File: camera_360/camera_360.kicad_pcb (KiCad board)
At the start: 2 copper layers, 58 x 46 mm, 20 parts, among them J1 usb_cam3, J2 usb_cam2, J3 usb_cam1, J5 usb_in, U1 CH334R, Y1 12Mhz

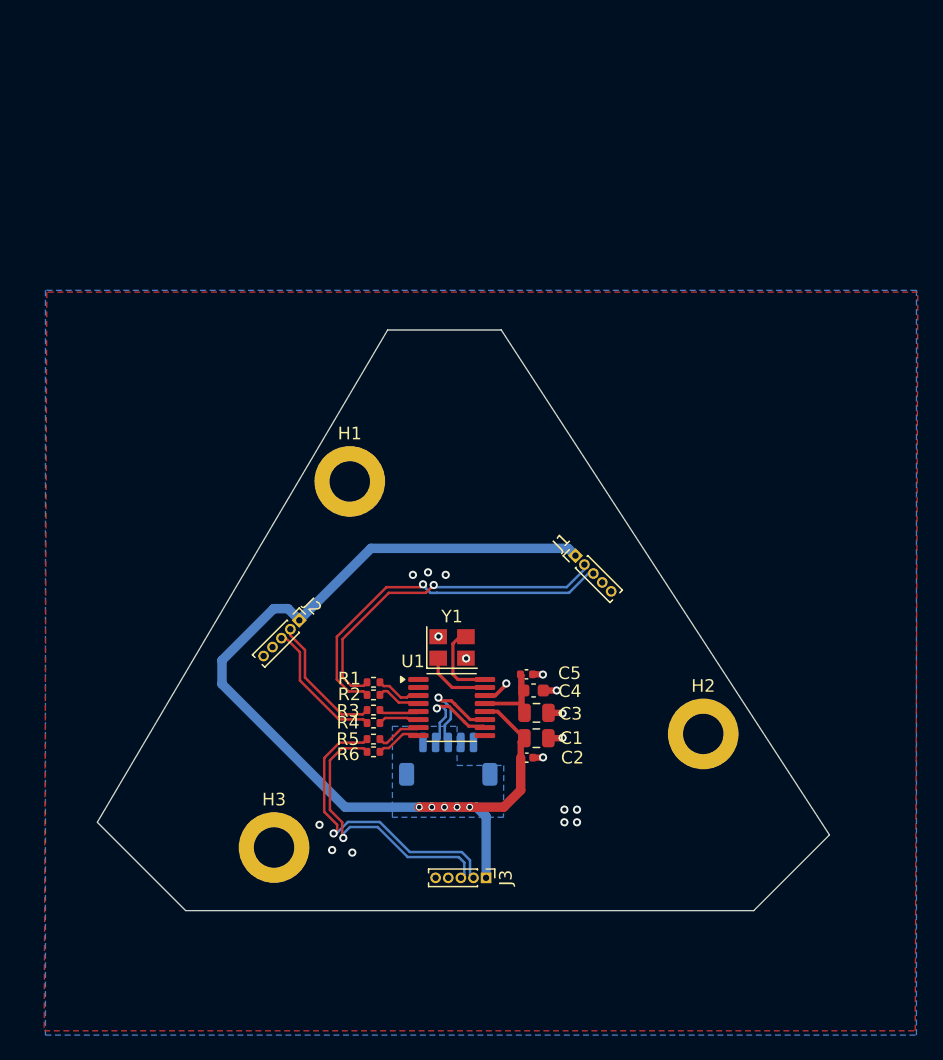
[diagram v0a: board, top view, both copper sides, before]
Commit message: REV 2. added usb c abd essd protection
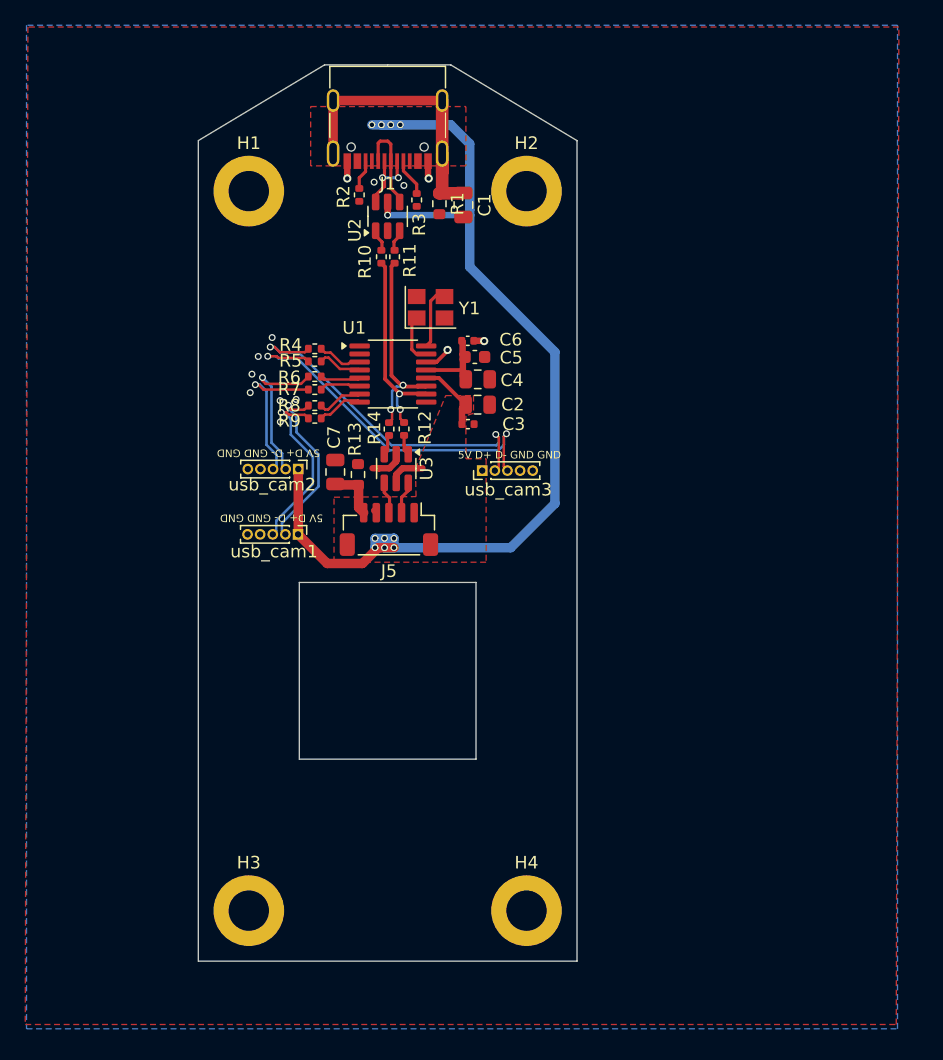
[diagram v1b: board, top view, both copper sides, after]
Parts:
- added C1: 10n, Capacitor_SMD:C_0805_2012Metric, F.Cu at (111.0, 45.1)
- added C7: 10n, Capacitor_SMD:C_0805_2012Metric, F.Cu at (100.8, 66.2)
- added H4: MountingHole, MountingHole:MountingHole_3.2mm_M3_DIN965_Pad, F.Cu at (116.0, 101.0)
- added J1: USB_C_Receptacle_USB2.0_14P, Connector_USB:USB_C_Receptacle_G-Switch_GT-USB-7010ASV, F.Cu at (105.0, 37.9)
- added R1: 33k, Resistor_SMD:R_0603_1608Metric, F.Cu at (109.1, 45.0)
- added R10: 22R, Resistor_SMD:R_0402_1005Metric, F.Cu at (104.5, 49.2)
- added R11: 22R, Resistor_SMD:R_0402_1005Metric, F.Cu at (105.5, 49.2)
- added R12: 22R, Resistor_SMD:R_0402_1005Metric, F.Cu at (106.3, 62.8)
- added R13: 33k, Resistor_SMD:R_0603_1608Metric, F.Cu at (102.7, 66.5)
- added R14: 22R, Resistor_SMD:R_0402_1005Metric, F.Cu at (105.1, 62.9)
- added R2: 4k7, Resistor_SMD:R_0402_1005Metric, F.Cu at (102.8, 44.3)
- added R3: 4k7, Resistor_SMD:R_0402_1005Metric, F.Cu at (107.3, 44.7)
- added U2: USBLC6-2SC6, Package_TO_SOT_SMD:SOT-23-6, F.Cu at (105.0, 46.0)
- added U3: USBLC6-2SC6, Package_TO_SOT_SMD:SOT-23-6, F.Cu at (105.7, 66.0)
- J5: moved to F.Cu
- moved H2 45.2 mm to (116.0, 44.0)
- moved usb_cam1 31.0 mm to (97.9, 71.2)
- moved Y1 27.0 mm to (108.4, 53.2)
- moved C2 26.8 mm to (112.1, 60.9)
- moved C5 26.8 mm to (111.9, 57.1)
- moved C6 26.8 mm to (111.3, 55.9)
- moved R9 26.8 mm to (99.2, 62.0)
- moved C3 26.8 mm to (111.4, 62.5)
- moved C4 26.8 mm to (112.1, 58.9)
- moved R4 26.8 mm to (99.2, 56.5)
- moved R5 26.8 mm to (99.2, 57.5)
- moved R6 26.8 mm to (99.2, 58.7)
- moved R7 26.8 mm to (99.2, 59.7)
- moved R8 26.8 mm to (99.2, 61.0)
- moved U1 26.8 mm to (105.4, 58.5)
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- renumbered C1 to C2, C2 to C3, C3 to C4, C4 to C5, C5 to C6, R1 to R4, R2 to R5, R3 to R6, R4 to R7, R5 to R8, R6 to R9, J3 to usb_cam1, J2 to usb_cam2, J1 to usb_cam3
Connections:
- J5 pad 2: /USB_UPSTREAM_D- -> /USB_CONN2_D-
- J5 pad 3: /USB_UPSTREAM_D+ -> /USB_CONN2_D+
- J5 pad 5: GND -> /SHIELD_CONN
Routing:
- net /SHIELD_USBC: track 0.00 -> 23.5 mm
- net /USB_CAM1-: track 24.5 -> 14.5 mm
- net +5V: track 81.5 -> 91.0 mm, vias 5 -> 11
- net /USB_CAM1+: track 22.7 -> 14.5 mm
- net /USB_CONN_D+: track 0.00 -> 7.46 mm
- net /USB_UPSTREAM_D-: track 8.36 -> 15.6 mm, vias 1 -> 2
- net /USB_UPSTREAM_D+: track 9.43 -> 16.6 mm, vias 1 -> 2
- net /USB_CONN_D-: track 0.00 -> 6.31 mm, vias 0 -> 2
- net /SHIELD_CONN: track 0.00 -> 4.22 mm
- net Net-(J1-CC1): track 0.00 -> 3.00 mm
- net /USB_CONN2_D-: track 0.00 -> 2.58 mm
- net /USB_CONN2_D+: track 0.00 -> 2.55 mm
- net Net-(J1-CC2): track 0.00 -> 2.37 mm
- net Net-(U1-XI): track 6.40 -> 4.46 mm
- net Net-(R10-Pad1): track 0.00 -> 1.78 mm
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- added copper zone on F.Cu, net +5V
- removed copper zone on B.Cu, net +5V
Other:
- board size 58 x 46 mm -> 30 x 71 mm
- board text added: "5V D+ D- GND GND"

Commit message: final revA
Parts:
- removed the R10 at (104.5, 49.2)
- removed the R11 at (105.5, 49.2)
- removed the R12 at (106.3, 62.8)
- removed the U2 at (105.0, 46.0)
- added C10: 100n, Capacitor_SMD:C_0603_1608Metric, F.Cu at (99.0, 46.5)
- added C11: 100n, Capacitor_SMD:C_0603_1608Metric, F.Cu at (92.0, 59.4)
- added C12: 10u, Capacitor_SMD:C_0805_2012Metric, F.Cu at (92.2, 55.6)
- added C13: 10u, Capacitor_SMD:C_0805_2012Metric, F.Cu at (92.2, 57.6)
- added C2: 100n, Capacitor_SMD:C_0402_1005Metric, F.Cu at (107.1, 52.3)
- added C3: 1n, Capacitor_SMD:C_0402_1005Metric, F.Cu at (108.1, 52.3)
- added C8: 10u, Capacitor_SMD:C_0805_2012Metric, F.Cu at (99.0, 44.5)
- added D1: SS22, Diode_SMD:D_SMA, F.Cu at (114.1, 49.2)
- added R13: 22R, Resistor_SMD:R_0402_1005Metric, F.Cu at (105.1, 67.2)
- added R2: 22R, Resistor_SMD:R_0402_1005Metric, F.Cu at (104.5, 45.2)
- added R3: 22R, Resistor_SMD:R_0402_1005Metric, F.Cu at (105.5, 45.2)
- added R4: 10k, Resistor_SMD:R_0402_1005Metric, F.Cu at (107.2, 53.8)
- added U1: TS3USB30EDGSR, Package_SO:VSSOP-10_3x3mm_P0.5mm, F.Cu at (103.0, 53.0)
- C7: renamed from C5; value 1u -> 10u; footprint Capacitor_SMD:C_0603_1608Metric -> Capacitor_SMD:C_0805_2012Metric
- U3: value USBLC6-2SC6 -> AZ1117-3.3; footprint Package_TO_SOT_SMD:SOT-23-6 -> Package_TO_SOT_SMD:SOT-223-3_TabPin2
- moved U3 18.5 mm to (94.8, 51.0), turned to 180 degrees
- moved R14 4.46 mm to (106.1, 67.2), turned to -90 degrees
- moved Y1 3.20 mm to (111.5, 54.0), turned to 90 degrees
- moved C6 1.53 mm to (111.8, 60.4)
- moved C4 1.52 mm to (111.8, 62.4)
- moved C5 1.48 mm to (111.0, 63.9)
- moved C7 1.26 mm to (111.8, 58.4)
- moved C9 1.07 mm to (111.1, 56.9)
- moved R5 0.25 mm to (103.0, 44.3)
- renumbered C7 to C14, C2 to C4, C3 to C5, C4 to C6, C6 to C9, usb_cam1 to J2, usb_cam2 to J3, usb_cam3 to J4, R7 to R10, R8 to R11, R9 to R12, R13 to R15, R2 to R5, R3 to R6, R4 to R7, R5 to R8, R6 to R9, U1 to U2
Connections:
- net /USB_CONN_D+ renamed Net-(J1-D+-PadA6)
- net /USB_CONN_D- renamed Net-(J1-D--PadA7)
- J1 pad A4: +5V -> /VBUS
- J1 pad A9: +5V -> /VBUS
- J1 pad B4: +5V -> /VBUS
- J1 pad B9: +5V -> /VBUS
- J5 pad 2: /USB_CONN2_D- -> Net-(J5-Pin_2)
- J5 pad 3: /USB_CONN2_D+ -> Net-(J5-Pin_3)
- R14 pad 1: Net-(R14-Pad1) -> /USB_PORT2_D-
- R14 pad 2: /USB_UPSTREAM_D+ -> Net-(J5-Pin_2)
- U3 pad 1: Net-(R12-Pad1) -> GND
- U3 pad 2: GND -> +3V3
- U3 pad 3: Net-(R14-Pad1) -> +5V
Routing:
- net /VBUS: track 0.00 -> 25.8 mm, vias 0 -> 2
- net +5V: track 91.0 -> 70.4 mm, vias 11 -> 13
- net /USB_CAM3+: track 29.4 -> 49.8 mm, vias 2 -> 1
- net /USB_CAM3-: track 28.6 -> 48.4 mm, vias 2 -> 1
- net +3V3: track 0.00 -> 19.8 mm
- net /USB_PORT2_D-: track 0.00 -> 17.3 mm, vias 0 -> 2
- net /USB_PORT2_D+: track 0.00 -> 17.3 mm, vias 0 -> 2
- net /USB_PORT1_D-: track 0.00 -> 12.2 mm, vias 0 -> 2
- net /USB_PORT1_D+: track 0.00 -> 11.2 mm, vias 0 -> 2
- net GND: track 8.63 -> 5.89 mm, vias 13 -> 25
- net /USB_UPSTREAM_D-: track 15.6 -> 13.0 mm
- net /USB_CONN2_D-: track 2.58 -> 0.00 mm
- net /USB_CONN2_D+: track 2.55 -> 0.00 mm
- net Net-(U1-~{OE}): track 0.00 -> 2.38 mm
- net /USB_UPSTREAM_D+: track 16.6 -> 14.3 mm
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- added copper zone on F.Cu, net +3V3
- added copper zone on F.Cu, net /VBUS
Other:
- outline, holes or cut-outs redrawn
- board text added: "GND GND D- D+ 5V"
- board text added: "USB IN"

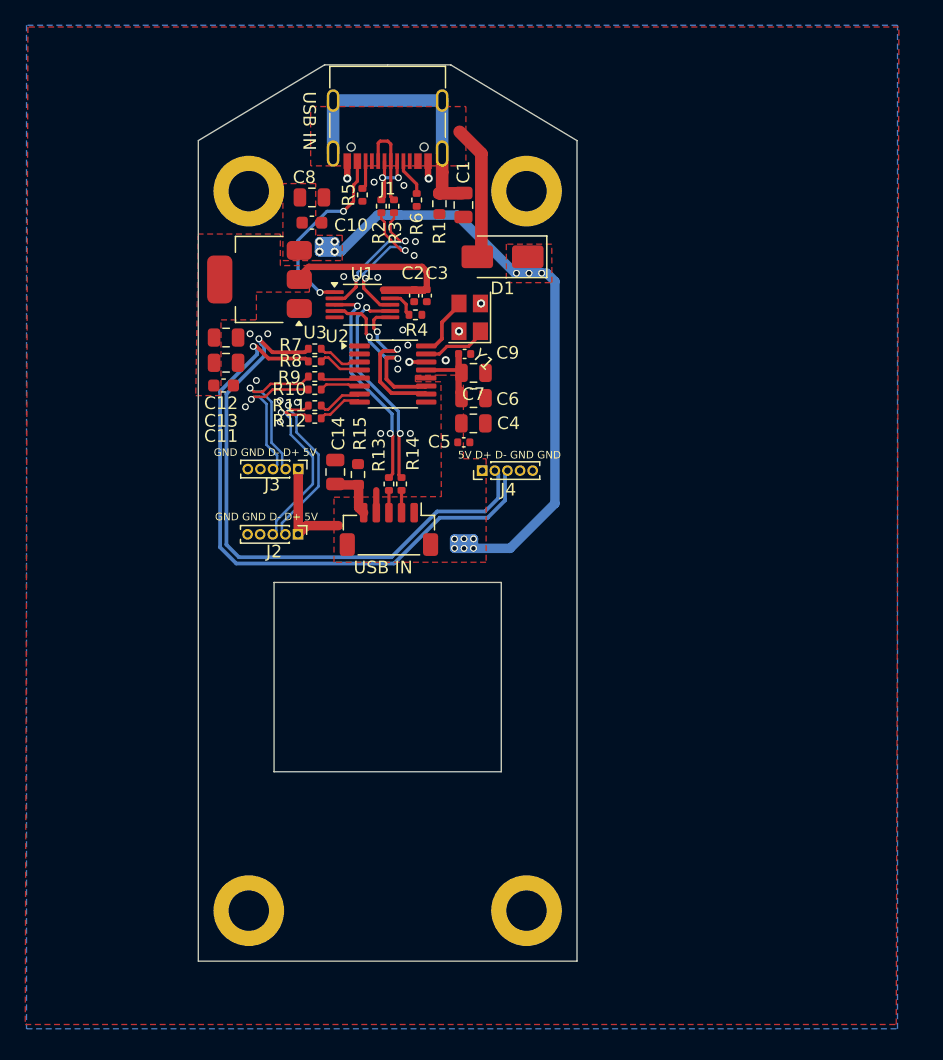
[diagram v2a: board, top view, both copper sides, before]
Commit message: update usb difff apirs and added vias
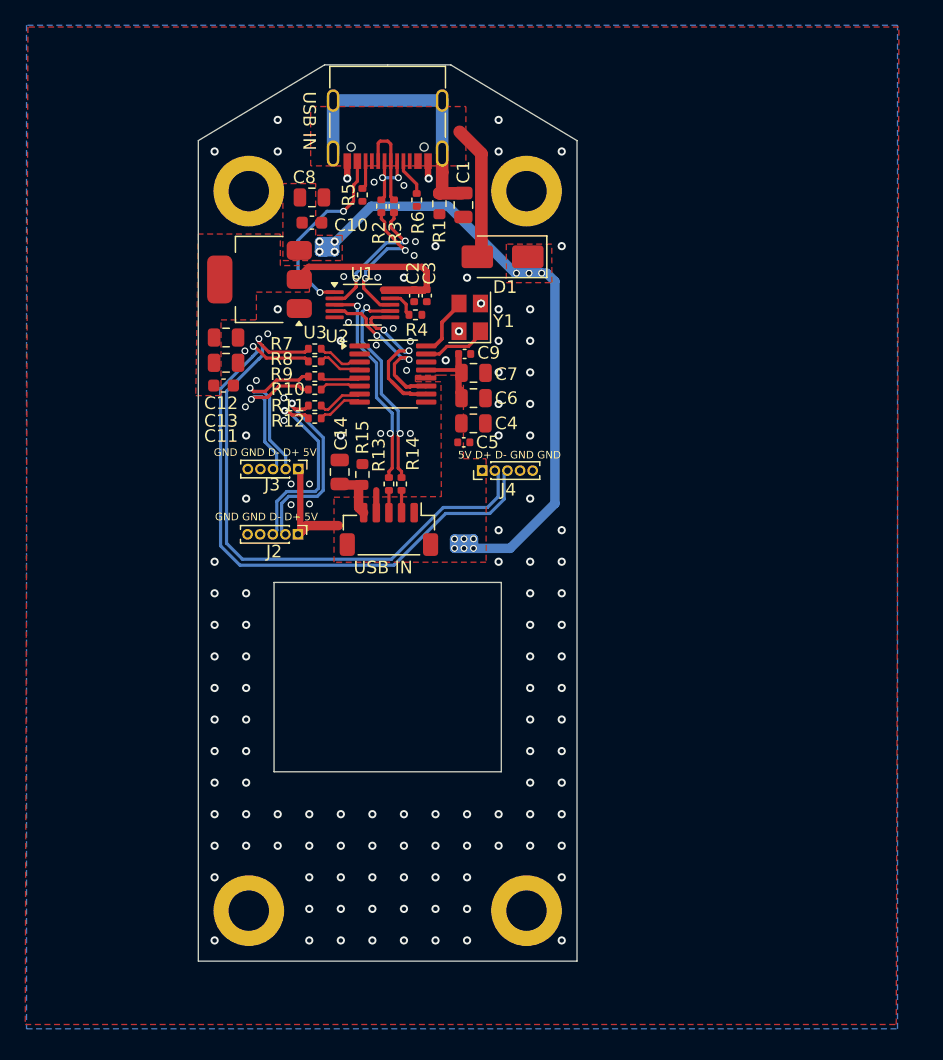
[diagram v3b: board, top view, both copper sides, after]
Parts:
- moved C14 0.35 mm to (101.2, 66.2)
- moved R15 0.35 mm to (103.0, 66.5)
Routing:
- net /USB_CAM1+: track 14.5 -> 16.0 mm
- net /USB_CAM1-: track 14.5 -> 15.9 mm
- net GND: track 5.89 -> 4.55 mm, vias 25 -> 135
- net /USB_UPSTREAM_D+: track 14.3 -> 13.7 mm

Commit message: Final rev
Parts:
- moved J4 16.3 mm to (97.8, 73.2), turned to -90 degrees
- moved J2 1.49 mm to (97.8, 69.7)
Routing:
- net /USB_CAM3+: track 49.7 -> 26.3 mm
- net /USB_CAM3-: track 48.4 -> 27.0 mm
- net +5V: track 70.5 -> 73.0 mm
- net /USB_CAM1+: track 16.0 -> 14.8 mm
- net /USB_CAM1-: track 15.9 -> 14.7 mm
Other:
- board text removed: "5V D+ D- GND GND"

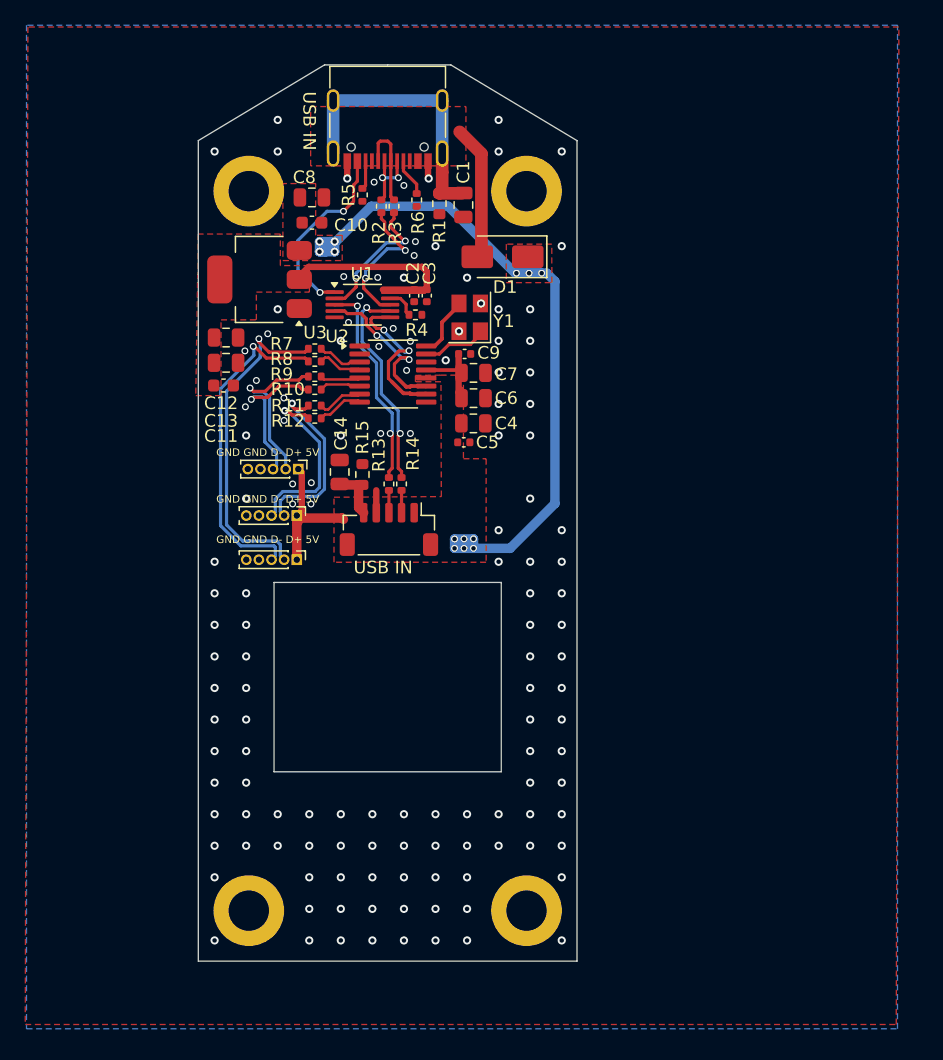
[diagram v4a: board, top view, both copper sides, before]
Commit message: chaged uusb connectro to jst mx1.25
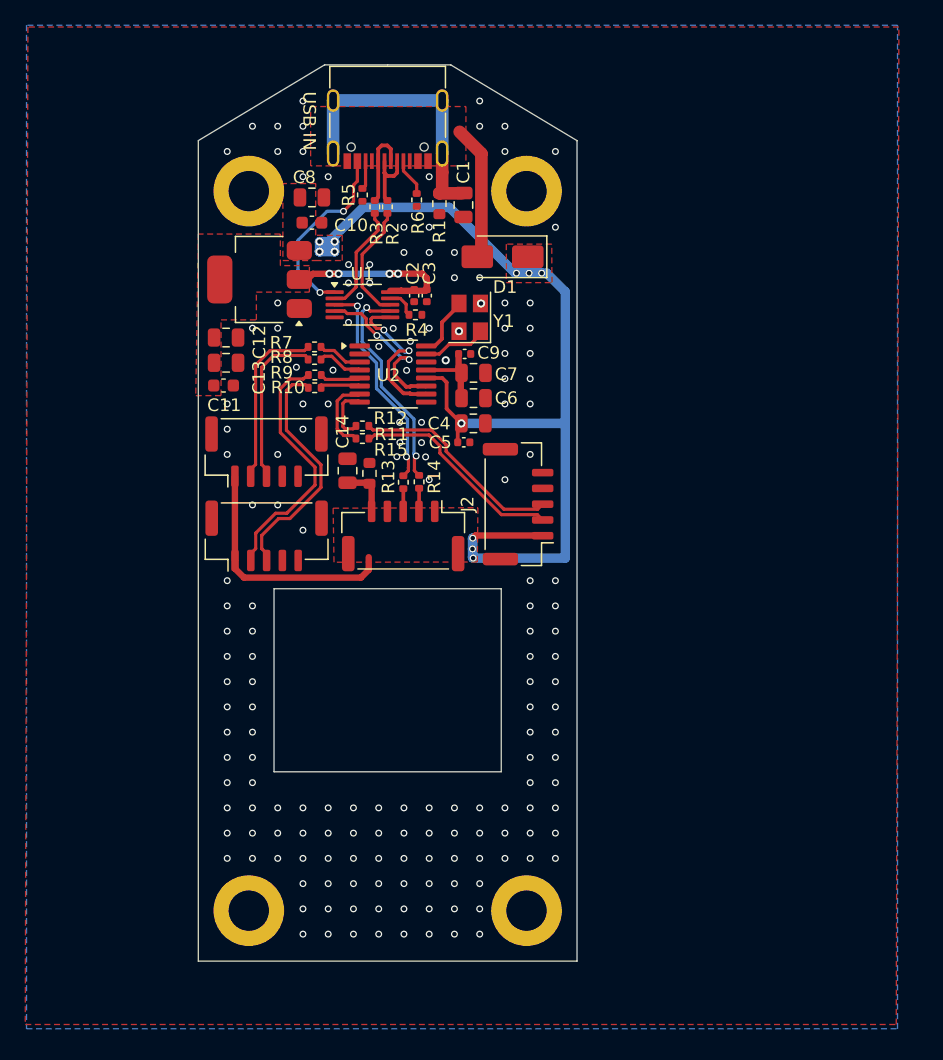
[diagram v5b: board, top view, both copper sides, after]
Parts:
- added kibuzzard-6782C80A: G***, kibuzzard-6782C80A, B.Cu at (95.7, 64.2)
- added kibuzzard-6782C81A: G***, kibuzzard-6782C81A, B.Cu at (95.6, 70.9)
- added kibuzzard-6782C82D: G***, kibuzzard-6782C82D, B.Cu at (115.4, 68.2)
- added kibuzzard-6782C8D8: G***, kibuzzard-6782C8D8, B.Cu at (105.0, 38.6)
- added kibuzzard-6782C8DC: G***, kibuzzard-6782C8DC, B.Cu at (106.2, 71.7)
- J2, J3, J4: footprint Connector_PinHeader_1.00mm:PinHeader_1x05_P1.00mm_Vertical -> Connector_JST:JST_GH_BM05B-GHS-TBT_1x05-1MP_P1.25mm_Vertical
- J5: footprint Connector_JST:JST_SH_BM05B-SRSS-TB_1x05-1MP_P1.00mm_Vertical -> Connector_JST:JST_GH_BM05B-GHS-TBT_1x05-1MP_P1.25mm_Vertical
- moved J2 17.6 mm to (115.3, 68.8), turned to 90 degrees
- moved J4 8.89 mm to (95.4, 64.6), turned to 0 degrees
- moved J3 5.86 mm to (95.4, 71.3), turned to 0 degrees
- moved R11 4.59 mm to (103.0, 63.6), turned to 0 degrees
- moved R12 3.82 mm to (103.0, 62.6), turned to 180 degrees
- moved R3 1.52 mm to (104.0, 45.2)
- moved R14 1.40 mm to (107.5, 67.0)
- moved J5 1.24 mm to (106.2, 71.3)
- moved R13 1.15 mm to (106.2, 67.1)
- moved C14 0.63 mm to (101.8, 66.2)
- moved R15 0.57 mm to (103.6, 66.4)
- moved R2 0.48 mm to (105.0, 45.2)
- moved R7 0.15 mm to (99.2, 56.3)
- moved R8 0.15 mm to (99.2, 57.3)
- moved R10 0.14 mm to (99.2, 59.6)
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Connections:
- J5 pad MP: (no net) -> GND
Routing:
- net +5V: track 73.0 -> 104.5 mm, vias 13 -> 11
- net /USB_CAM3+: track 26.3 -> 12.9 mm, vias 1 -> 0
- net /USB_CAM3-: track 27.0 -> 13.7 mm, vias 1 -> 0
- net /USB_CAM2+: track 12.3 -> 19.3 mm, vias 1 -> 0
- net /USB_CAM2-: track 13.3 -> 20.0 mm, vias 1 -> 0
- net GND: track 4.55 -> 0.00 mm, vias 135 -> 172
- net +3V3: track 19.8 -> 15.7 mm, vias 0 -> 4
- net /USB_PORT1_D-: track 11.8 -> 9.46 mm, vias 2 -> 0
- net Net-(U2-DM1): track 3.68 -> 6.02 mm
- net /USB_CAM1-: track 14.7 -> 17.0 mm, vias 1 -> 0
- net /USB_CAM1+: track 14.8 -> 17.0 mm, vias 1 -> 0
- net /USB_PORT1_D+: track 11.0 -> 9.00 mm, vias 2 -> 0
- net Net-(U2-VDD33): track 7.21 -> 6.25 mm
- net Net-(U2-DP1): track 3.68 -> 4.48 mm
- net Net-(J1-D--PadA7): track 5.95 -> 5.34 mm, vias 2 -> 0
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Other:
- outline, holes or cut-outs redrawn
- board text removed: "GND GND D- D+ 5V"
